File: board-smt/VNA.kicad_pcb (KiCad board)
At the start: 2 copper layers, 100 x 100 mm, 171 parts, among them J1 Conn_02x07_Odd_Even, J10 Conn_01x01, J11 Conn_01x01, J12 Conn_01x01, J13 Barrel_Jack, J14 Conn_01x01, J15 Conn_01x02, J16 Conn_01x01, J17 Conn_01x04, J18 Conn_01x01, J19 Conn_01x01, J2 Conn_Coaxial, J20 Conn_01x01, J21 Conn_01x01, J22 Conn_01x02, J24 USB_B, J3 Conn_01x01, J4 Conn_01x01, J5 Conn_01x01, J6 Conn_01x01, J7 Conn_01x01, J8 Conn_01x01, J9 Conn_Coaxial, Q3 S9018, SW1 SW_DPDT_x2, U1 SI5351A, U10 MT3608, U11 CN3052, U12 SI5351A, U2 LM339, U3 SA612, U4 SA612, U5 SA612, U6 LM358, U7 LM358, U8 AMS1117-3V3, U9 78M05_TO252, Y1 27 MHz

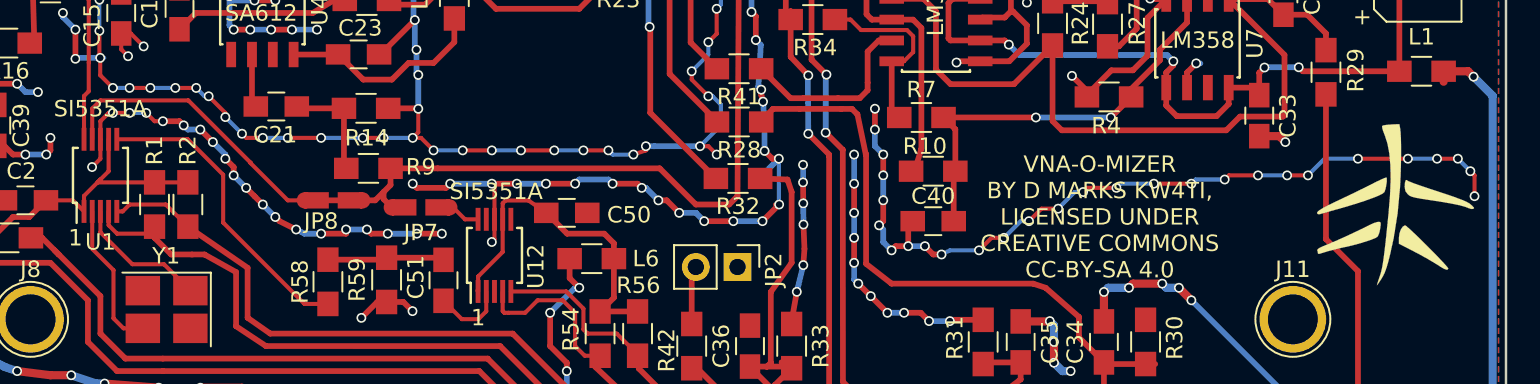
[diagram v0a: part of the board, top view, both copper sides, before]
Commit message: Added source termination resistor to LO SI5351A
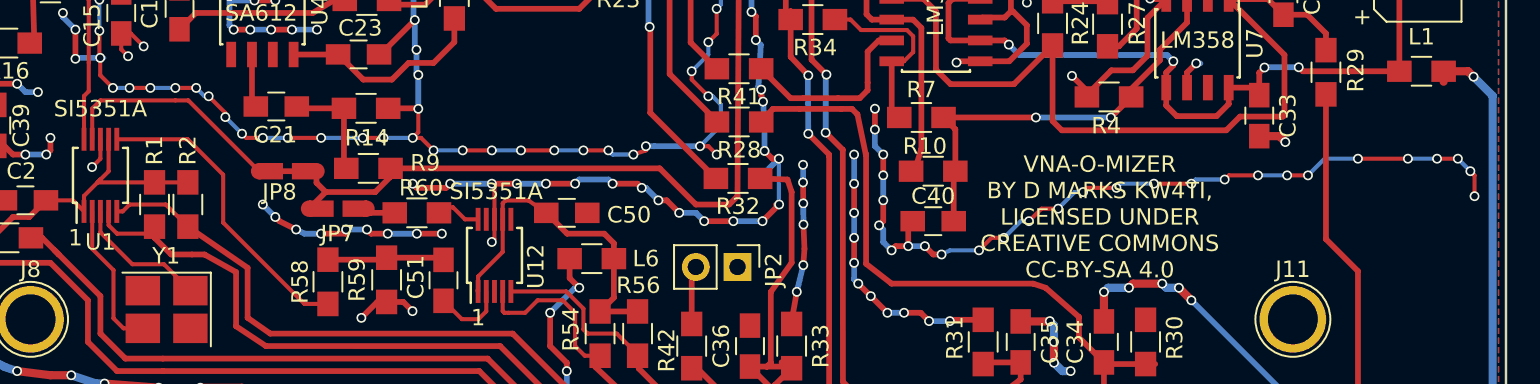
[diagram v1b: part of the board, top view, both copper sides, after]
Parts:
- removed G***: LOGO, VNA:VNAOMizer
- added R60: 68R, Resistors_SMD:R_0805_HandSoldering, F.Cu at (83.6, 95.5)
- moved JP7 5.05 mm to (78.7, 95.2)
- moved JP8 3.31 mm to (75.7, 93.0)
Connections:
- U12 pad 10: Net-(JP7-Pad1) -> Net-(R60-Pad2)
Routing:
- net GND: track 1355.9 -> 1330.1 mm, vias 529 -> 510
- net (no net): track 0.00 -> 11.9 mm, vias 0 -> 9
- net Net-(R60-Pad2): track 0.00 -> 2.06 mm

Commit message: Changes to finalize two SI5351A solution
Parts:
- removed JP7: Jumper_NO_Small, VNA:PAD_DEFAULT_OPEN
- removed JP8: Jumper_NC_Small, VNA:PAD_DEFAULT_OPEN
- added C52: 100 uF, Capacitors_SMD:CP_Elec_4x4.5, F.Cu at (66.1, 144.9)
- added JP9: Jumper_NC_Small, Pin_Headers:Pin_Header_Straight_1x02_Pitch2.54mm, F.Cu at (75.7, 133.7)
- L9: value 100 uH -> 10 uH
- moved C43 10.6 mm to (82.1, 128.2), turned to 90 degrees
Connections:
- J24 pad 1: POWFILT -> Net-(J24-Pad1)
- R43 pad 2: Net-(JP7-Pad2) -> Net-(R43-Pad2)
- R45 pad 2: Net-(JP7-Pad2) -> Net-(R43-Pad2)
- R60 pad 1: Net-(JP7-Pad1) -> Net-(R43-Pad2)
- R9 pad 2: Net-(JP7-Pad2) -> Net-(R43-Pad2)
- U1 pad 9: Net-(JP7-Pad2) -> (no net)
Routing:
- net Net-(JP7-Pad2): track 91.4 -> 0.00 mm
- net Net-(R43-Pad2): track 0.00 -> 70.8 mm
- net GND: track 1330.1 -> 1360.9 mm, vias 510 -> 524
- net POWFILT: track 99.4 -> 74.2 mm, vias 2 -> 0
- net (no net): track 11.9 -> 0.00 mm, vias 9 -> 0
- net Net-(J24-Pad1): track 0.00 -> 8.81 mm
- net +5V: track 234.7 -> 226.4 mm
- net Net-(JP7-Pad1): track 1.83 -> 0.00 mm

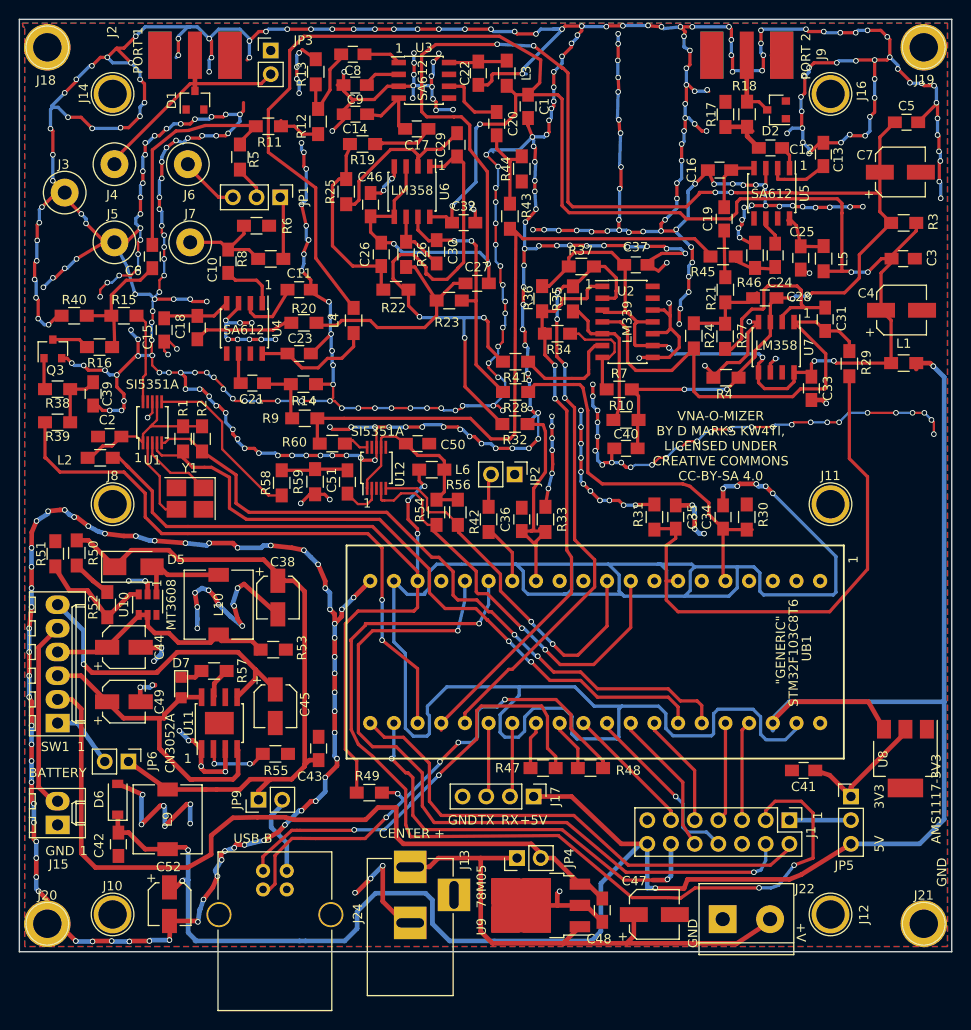
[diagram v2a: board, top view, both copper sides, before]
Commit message: Shrank the SMT board by 15 mm
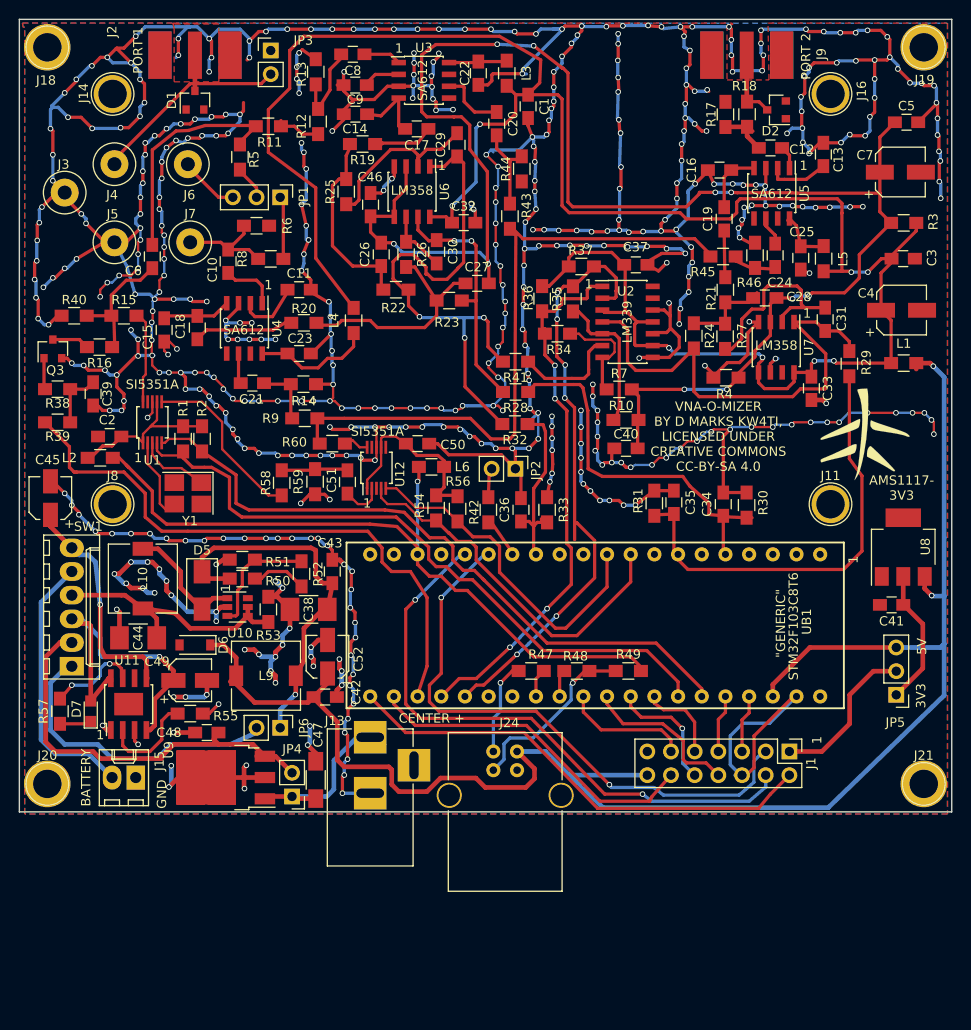
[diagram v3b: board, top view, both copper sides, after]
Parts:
- removed J10, J12: Conn_01x01, Connectors:1pin
- removed J17: Conn_01x04, Pin_Headers:Pin_Header_Straight_1x04_Pitch2.54mm
- removed J22: Conn_01x02, Connectors_Terminal_Blocks:TerminalBlock_bornier-2_P5.08mm
- removed JP9: Jumper_NC_Small, Pin_Headers:Pin_Header_Straight_1x02_Pitch2.54mm
- added G***: LOGO, VNA:VNAOMizer, F.Cu at (140.7, 94.5)
- C38, C44: footprint Capacitors_SMD:CP_Elec_4x4.5 -> Capacitors_SMD:C_1210_HandSoldering
- C47: value 100 uF -> 330 nF; footprint Capacitors_SMD:CP_Elec_5x5.3 -> Capacitors_SMD:C_1206_HandSoldering
- moved C48 46.5 mm to (70.1, 126.5), turned to 180 degrees
- moved C47 39.1 mm to (81.8, 131.6), turned to 90 degrees
- moved U9 36.5 mm to (72.1, 131.3)
- moved C45 32.9 mm to (53.3, 101.3), turned to 90 degrees
- moved C52 31.5 mm to (83.1, 118.4), turned to 90 degrees
- moved R49 30.7 mm to (115.3, 119.9), turned to 180 degrees
- moved J24 27.8 mm to (103.4, 128.5)
- moved C42 27.2 mm to (82.8, 122.7), turned to 0 degrees
- moved JP4 25.0 mm to (79.2, 133.3), turned to 180 degrees
- moved U8 22.7 mm to (144.8, 106.6), turned to 90 degrees
- moved R52 21.1 mm to (80.3, 109.5), turned to 270 degrees
- moved C41 20.1 mm to (143.6, 112.8)
- moved R51 20.1 mm to (73.9, 108.0), turned to 0 degrees
- moved C43 19.0 mm to (83.6, 109.2)
- moved L9 18.7 mm to (76.5, 120.4), turned to 0 degrees
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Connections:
- J24 pad 1: Net-(J24-Pad1) -> +5V
- UB1 pad 30: Net-(J17-Pad3) -> (no net)
- UB1 pad 31: Net-(J17-Pad2) -> (no net)
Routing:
- net GND: track 1360.9 -> 1109.8 mm, vias 524 -> 499
- net +5V: track 226.4 -> 181.9 mm, vias 4 -> 2
- net PB10: track 102.1 -> 62.7 mm, vias 3 -> 2
- net REG5VOUT: track 84.8 -> 45.9 mm
- net Net-(C47-Pad1): track 58.2 -> 20.3 mm
- net Net-(J24-Pad2): track 47.2 -> 10.2 mm, vias 2 -> 1
- net Net-(J24-Pad3): track 55.6 -> 19.5 mm, vias 5 -> 1
- net POWFILT: track 74.2 -> 40.9 mm, vias 0 -> 1
- net Net-(JP6-Pad2): track 7.96 -> 32.9 mm
- net PB11: track 80.5 -> 63.8 mm
- net Net-(C45-Pad1): track 36.2 -> 24.6 mm
- net Net-(J1-Pad1): track 6.60 -> 16.8 mm
- net DEMODCUR2: track 57.4 -> 47.4 mm
- net Net-(J24-Pad1): track 8.81 -> 0.00 mm
- net Net-(J1-Pad12): track 45.4 -> 36.8 mm, vias 2 -> 0
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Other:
- board size 100 x 100 mm -> 100 x 85 mm
- board text added: "AMS1117- 3V3"
- board text removed: "+5V"
- board text removed: "+V"
- board text removed: "78M05"
- board text removed: "AMS1117-3V3"
- board text removed: "CN3052A"
- board text removed: "MT3608"
- board text removed: "RX"
- board text removed: "TX"
- board text removed: "USB B"

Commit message: Made a little space around external connectors
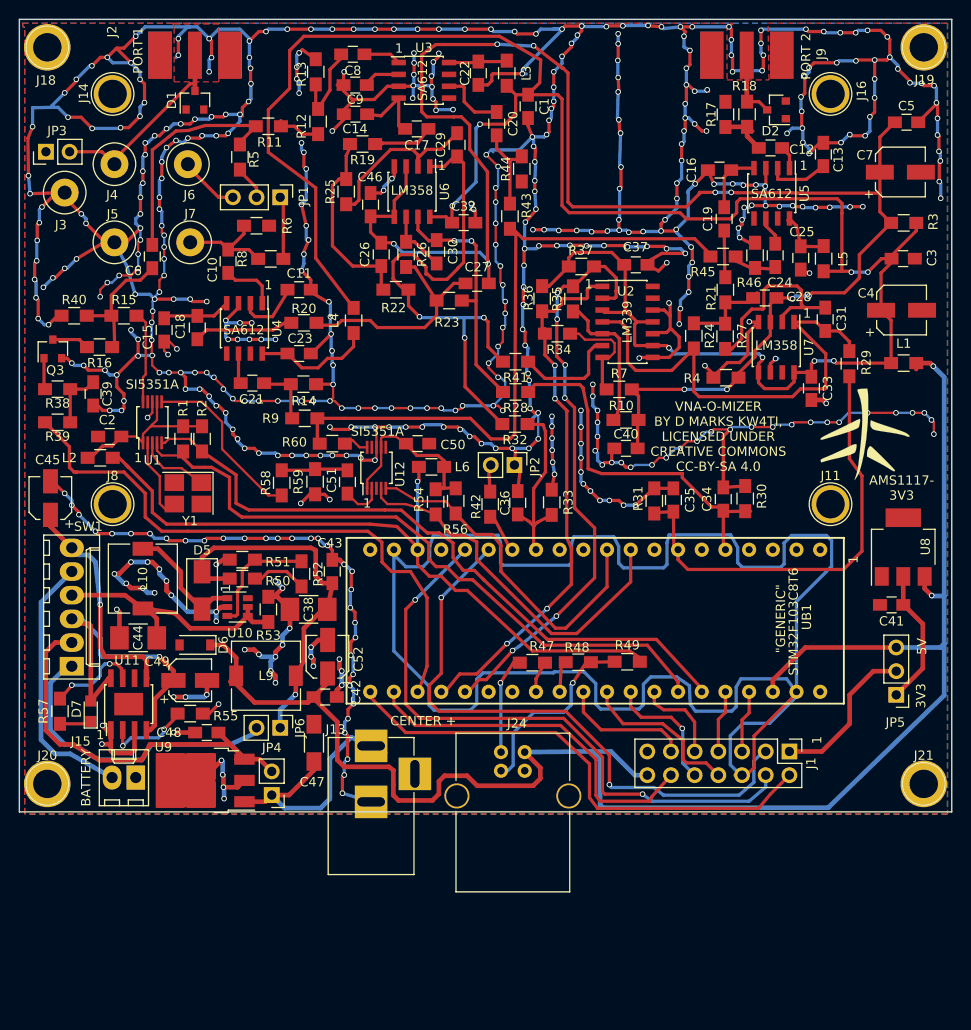
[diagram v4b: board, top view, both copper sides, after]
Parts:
- moved JP3 26.4 mm to (52.9, 64.2), turned to 90 degrees
- moved C47 3.98 mm to (81.6, 127.6)
- moved U9 2.22 mm to (69.9, 131.6)
- moved JP4 2.18 mm to (77.1, 133.2)
- moved R49 0.99 mm to (115.2, 118.9)
- moved R48 0.95 mm to (110.0, 119.0)
- moved R33 0.94 mm to (107.1, 101.8)
- moved J13 0.93 mm to (87.7, 127.9)
- moved R47 0.90 mm to (105.0, 119.0)
- moved R56 0.87 mm to (96.8, 101.7)
- moved C36 0.83 mm to (103.5, 101.8)
- moved J24 0.82 mm to (104.2, 128.6)
- moved R30 0.72 mm to (127.8, 101.4)
- moved R54 0.65 mm to (94.7, 101.8)
- moved R42 0.63 mm to (100.5, 102.0)
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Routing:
- net GND: track 1109.8 -> 1267.3 mm, vias 499 -> 500
- net Net-(C47-Pad1): track 20.3 -> 31.8 mm
- net Net-(D1-Pad3): track 27.2 -> 22.7 mm
- net +5V: track 181.9 -> 185.2 mm
- net Net-(J1-Pad12): track 36.8 -> 39.0 mm
- net PB11: track 63.8 -> 65.9 mm
- net PB12: track 52.2 -> 54.3 mm
- net SYNCSAMPLE2: track 64.9 -> 63.0 mm
- net REG5VOUT: track 45.9 -> 44.1 mm
- net Net-(J24-Pad3): track 19.5 -> 20.9 mm
- net PB10: track 62.7 -> 64.0 mm
- net Net-(R55-Pad2): track 10.7 -> 9.41 mm, vias 0 -> 2
- net Net-(R48-Pad1): track 3.38 -> 4.32 mm
- net Net-(R47-Pad1): track 3.08 -> 3.87 mm
- net +3V3: track 78.4 -> 77.7 mm
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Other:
- board text removed: "GND"

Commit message: Moved mounting holes slightly
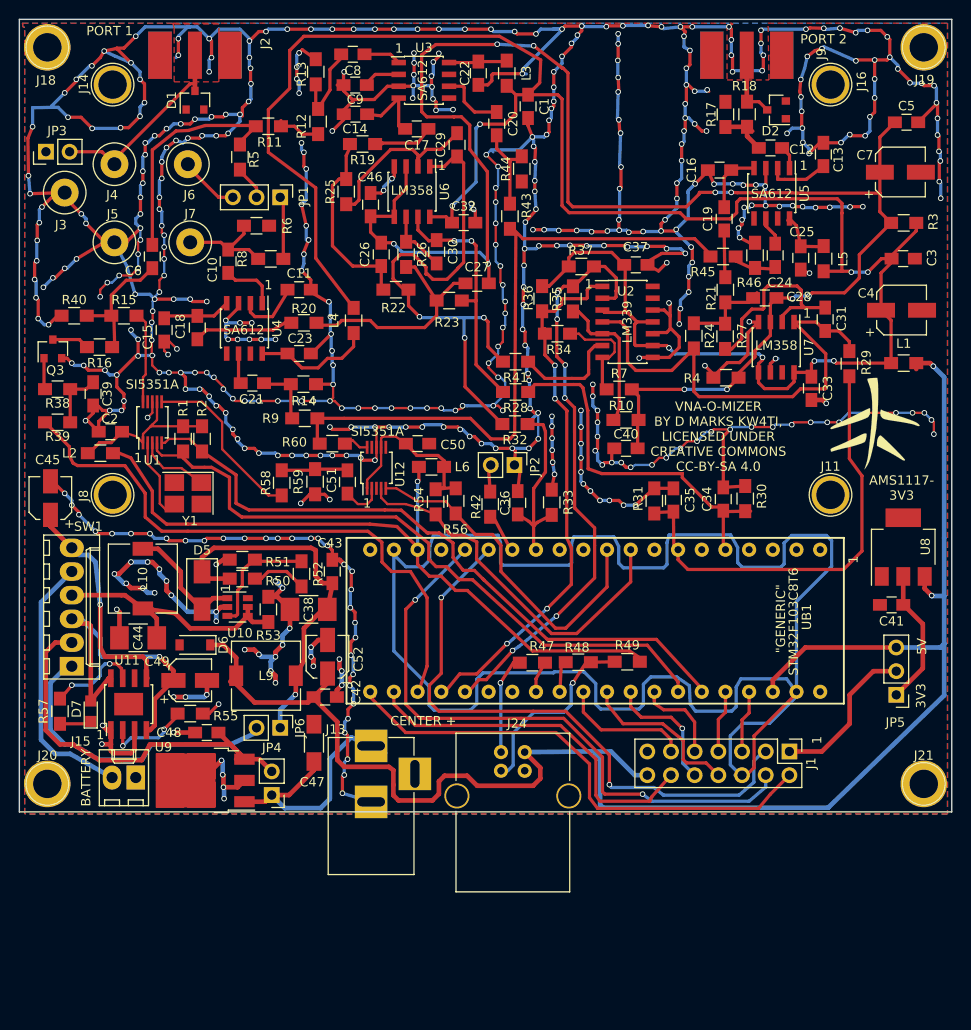
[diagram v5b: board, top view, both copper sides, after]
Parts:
- moved G*** 1.57 mm to (141.8, 93.3)
- moved J11 1.00 mm to (137.0, 101.0)
- moved J14 1.00 mm to (60.0, 57.0)
- moved J16 1.00 mm to (137.0, 57.0)
- moved J8 1.00 mm to (60.0, 101.0)
- moved C2 0.52 mm to (59.8, 94.2)
- moved L2 0.50 mm to (58.7, 96.5)
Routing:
- net GND: track 1267.3 -> 1275.9 mm, vias 500 -> 501

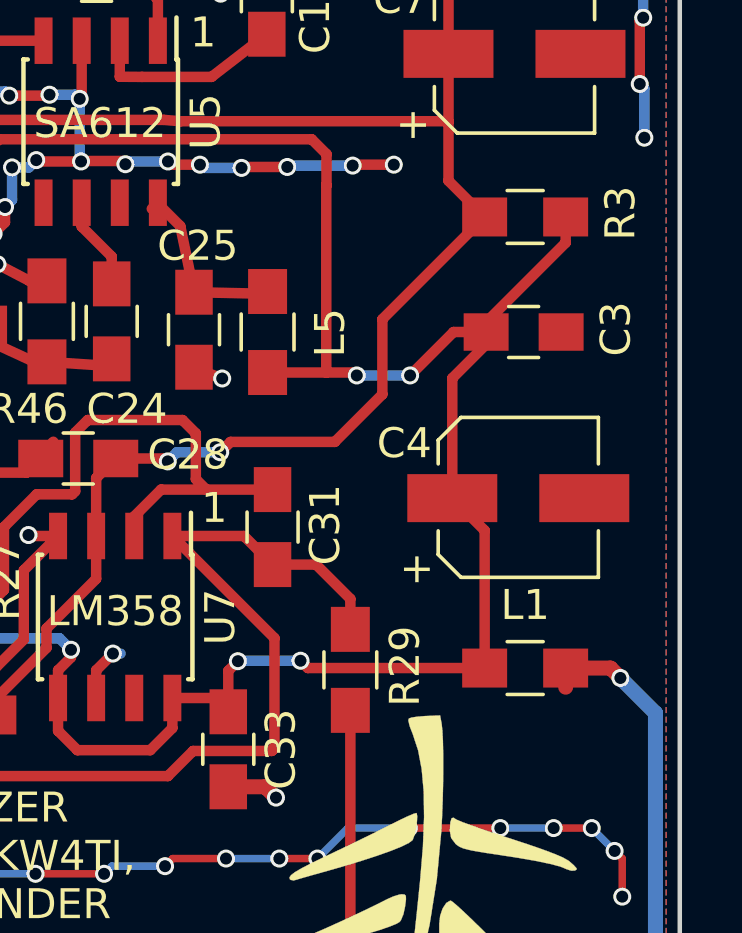
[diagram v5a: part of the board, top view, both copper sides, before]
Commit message: Bigger footprint for C4
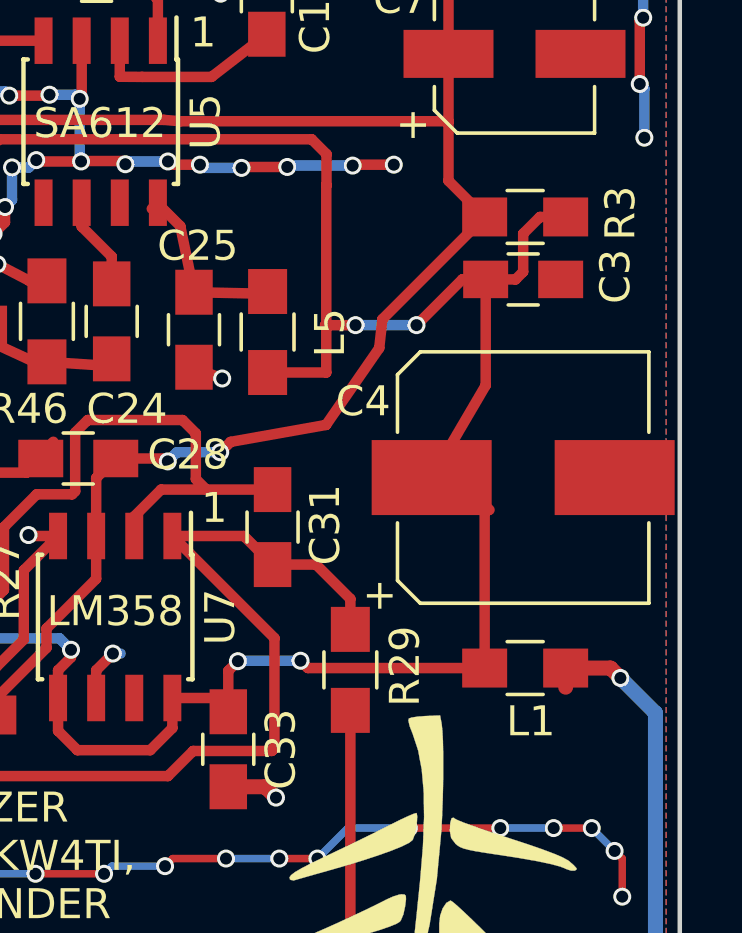
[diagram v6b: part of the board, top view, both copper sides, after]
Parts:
- C4: footprint Capacitors_SMD:CP_Elec_5x5.3 -> Capacitors_SMD:CP_Elec_8x10.5
- moved C3 1.75 mm to (144.8, 73.9)
- moved C4 0.70 mm to (144.8, 80.5)
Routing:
- net FILT5V: track 228.9 -> 232.9 mm
- net 2V0: track 178.0 -> 177.1 mm

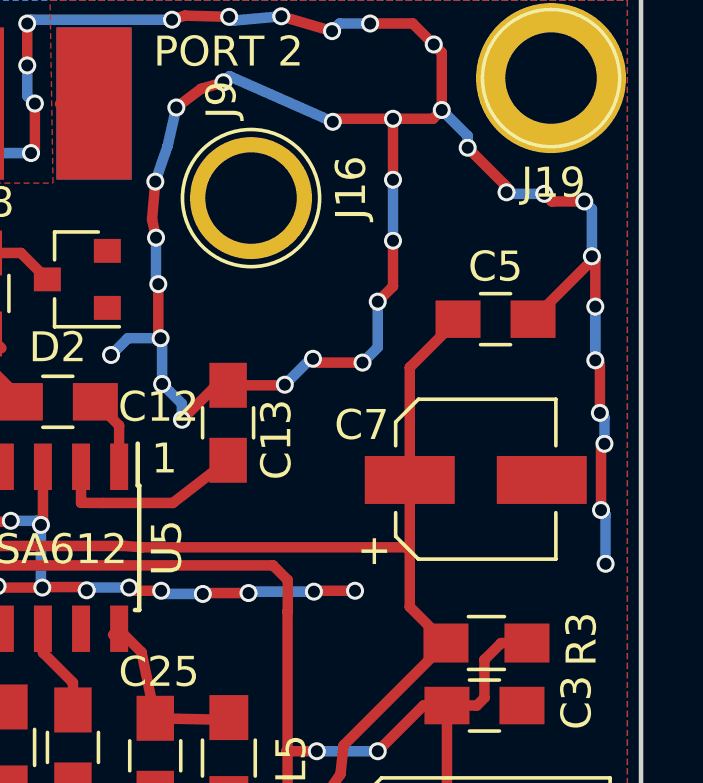
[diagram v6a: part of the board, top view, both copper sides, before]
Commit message: Updated software to add cursor for smith chart, also changed edge of triggering
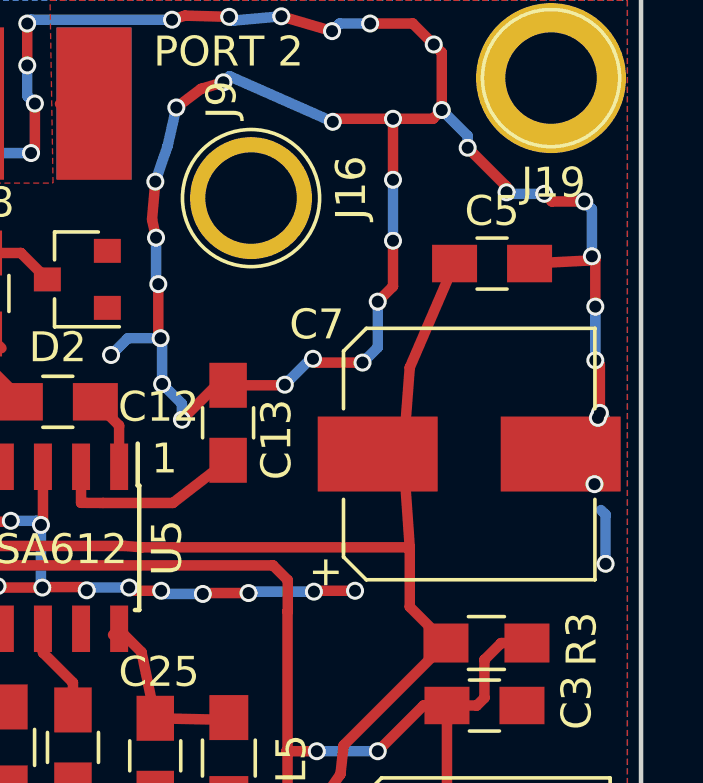
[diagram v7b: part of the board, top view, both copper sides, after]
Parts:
- C4: value 100 uF -> 1000 uF
- C7: value 10 uF -> 1000 uF; footprint Capacitors_SMD:CP_Elec_5x5.3 -> Capacitors_SMD:CP_Elec_8x10.5
- R36, R37: value 1k -> 10k
- moved C5 1.86 mm to (145.0, 59.2)
- moved C7 0.89 mm to (144.3, 65.5)
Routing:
- net GND: track 1275.9 -> 1273.3 mm, vias 501 -> 500
- net (no net): track 0.00 -> 1.85 mm, vias 0 -> 1
- net 2V0: track 177.1 -> 178.6 mm
